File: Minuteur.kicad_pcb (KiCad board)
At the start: 2 copper layers, 149.9 x 49.5 mm, 47 parts, among them J1 ICSP, J2 Screw_Terminal_1x02, J3 Piezo, J4 Inputs, J5 Data, J6 USB_OTG, J7 Screw_Terminal_1x03, J8 Outputs, Q1 BC818-40, SW1 Rotary_Encoder_Switch, SW2 SW_Push_SPDT_2Leds, SW3 SW_Push_SPDT_2Leds, U1 ATMEGA328P-AU, U2 LD1117S50TR, U3 MAX7219, U4 PC817, Y1 16MHz

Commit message: General layout done.
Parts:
- removed AFF1: CC56-12, Displays_7-Segment:Cx56-12
- removed D3: LED, LEDs:LED_0805
- removed D4: D, Diodes_SMD:D_SOD-123
- removed J7: Screw_Terminal_1x03, Connectors:bornier3
- removed J8: Outputs, Pin_Headers:Pin_Header_Straight_1x04_Pitch2.54mm
- removed R11, R12: 470, Resistors_SMD:R_0805
- removed REF** (x4): MountingHole_3.2mm_M3_Pad, Mounting_Holes:MountingHole_3.2mm_M3_Pad
- removed REF** (x2): Fiducial_1mm_Dia_2.54mm_Outer_CopperTop, Fiducials:Fiducial_1mm_Dia_2.54mm_Outer_CopperTop
- removed REF**: Logo_labo_20mm, Logos:Logo_labo_20mm
- removed SW3: SW_Push_SPDT_2Leds, Switches_perso:SP86-THT-PushButton
- added C6: 100n, Capacitor_SMD:C_0805_2012Metric, F.Cu at (189.5, 93.5)
- added FID1: Fiducial, Fiducial:Fiducial_0.75mm_Mask1.5mm, F.Cu at (187.9, 147.0)
- added FID2: Fiducial, Fiducial:Fiducial_0.75mm_Mask1.5mm, F.Cu at (191.0, 147.0)
- added FID3: Fiducial, Fiducial:Fiducial_0.75mm_Mask1.5mm, F.Cu at (194.0, 147.0)
- added FID4: Fiducial, Fiducial:Fiducial_0.75mm_Mask1.5mm, F.Cu at (187.9, 150.1)
- added FID5: Fiducial, Fiducial:Fiducial_0.75mm_Mask1.5mm, F.Cu at (191.0, 150.1)
- added FID6: Fiducial, Fiducial:Fiducial_0.75mm_Mask1.5mm, F.Cu at (187.9, 153.1)
- added H1: MountingHole, MountingHole:MountingHole_3.2mm_M3, F.Cu at (93.0, 72.0)
- added H2: MountingHole, MountingHole:MountingHole_3.2mm_M3, F.Cu at (203.0, 72.0)
- added H3: MountingHole, MountingHole:MountingHole_3.2mm_M3, F.Cu at (203.0, 112.0)
- added H4: MountingHole, MountingHole:MountingHole_3.2mm_M3, F.Cu at (93.0, 112.0)
- added U5: CC56-12EWA, Display_7Segment:CA56-12EWA, B.Cu at (180.0, 93.0)
- C1, C5: footprint Capacitors_SMD:C_0805 -> Capacitor_SMD:C_0805_2012Metric
- C2: value 47u -> 100n; footprint Capacitors_SMD:CP_Elec_6.3x5.3 -> Capacitor_SMD:C_0805_2012Metric
- C3: footprint Capacitors_SMD:CP_Elec_6.3x5.3 -> Capacitor_SMD:CP_Elec_6.3x5.3
- C4: value 100n -> 47u; footprint Capacitors_SMD:C_0805 -> Capacitor_SMD:CP_Elec_6.3x5.3
- D1: footprint Diodes_SMD:D_SOD-123 -> Diode_SMD:D_SOD-123
- D2: value LED -> D; footprint LEDs:LED_0805 -> Diode_SMD:D_SOD-123
- J1: value ICSP -> Screw_Terminal_01x02; footprint Connectors:IDC_Header_Straight_6pins -> Connector_Phoenix_MSTB:PhoenixContact_MSTBVA_2,5_2-G-5,08_1x02_P5.08mm_Vertical
- J2: value Screw_Terminal_1x02 -> ICSP; footprint Connectors:bornier2 -> Connector_PinHeader_2.54mm:PinHeader_2x03_P2.54mm_Vertical
- J3: value Piezo -> piezo; footprint Pin_Headers:Pin_Header_Straight_1x02_Pitch2.54mm -> Connector_PinHeader_2.54mm:PinHeader_1x02_P2.54mm_Vertical
- J4: value Inputs -> Conn_01x10; footprint Pin_Headers:Pin_Header_Straight_1x07_Pitch2.54mm -> Connector_PinHeader_2.54mm:PinHeader_1x10_P2.54mm_Vertical
- J5: value Data -> output; footprint Pin_Headers:Pin_Header_Straight_1x06_Pitch2.54mm -> Connector_PinHeader_2.54mm:PinHeader_1x04_P2.54mm_Vertical
- J6: value USB_OTG -> Screw_Terminal_01x03; footprint Connectors:USB_Micro-B -> Connector_Phoenix_MSTB:PhoenixContact_MSTBVA_2,5_3-G-5,08_1x03_P5.08mm_Vertical
- Q1: value BC818-40 -> BC818; footprint TO_SOT_Packages_SMD:SOT-23 -> Package_TO_SOT_SMD:SOT-23
- R1, R4: footprint Resistors_SMD:R_0805 -> Resistor_SMD:R_0805_2012Metric
- R10: value 510 -> 470; footprint Resistors_SMD:R_0805 -> Resistor_SMD:R_0805_2012Metric
- R2: value 10K -> 10k; footprint Resistors_SMD:R_0805 -> Resistor_SMD:R_0805_2012Metric
- R3: value 1K -> 470; footprint Resistors_SMD:R_0805 -> Resistor_SMD:R_0805_2012Metric
- R5: value 470 -> 30k; footprint Resistors_SMD:R_0805 -> Resistor_SMD:R_0805_2012Metric
- R6: value 30K -> 470; footprint Resistors_SMD:R_0805 -> Resistor_SMD:R_0805_2012Metric
- R7: value 470 -> 1k; footprint Resistors_SMD:R_0805 -> Resistor_SMD:R_0805_2012Metric
- R8: value 1K -> 1k; footprint Resistors_SMD:R_0805 -> Resistor_SMD:R_0805_2012Metric
- R9: value 1K -> 510; footprint Resistors_SMD:R_0805 -> Resistor_SMD:R_0805_2012Metric
- RL1: footprint Relays_THT:Relay_SPDT_SANYOU_SRD_Series_Form_C -> Relay_THT:Relay_SPDT_SANYOU_SRD_Series_Form_C; moved to F.Cu
- SW1: footprint Switches_perso:EC12_switch-RotaryEncoder -> Rotary_Encoder:RotaryEncoder_Alps_EC12E-Switch_Vertical_H20mm_CircularMountingHoles; moved to B.Cu
- SW2: footprint Switches_perso:SP86-THT-PushButton -> Switch_Perso:SP86-THT-PushButton; moved to B.Cu
- U1: value ATMEGA328P-AU -> ATmega328P-AU; footprint Housings_QFP:TQFP-32_7x7mm_Pitch0.8mm -> Package_QFP:TQFP-32_7x7mm_P0.8mm
- U2: value LD1117S50TR -> LD1117S50TR_SOT223; footprint TO_SOT_Packages_SMD:SOT-223-3Lead_TabPin2 -> Package_TO_SOT_SMD:SOT-223-3_TabPin2
- U3: footprint Housings_SOIC:SOIC-24W_7.5x15.4mm_Pitch1.27mm -> Package_SO:SOIC-24W_7.5x15.4mm_P1.27mm
- U4: footprint Housings_DIP:DIP-4_W7.62mm_SMD -> Package_DIP:DIP-4_W7.62mm
- Y1: footprint SMD_perso:Resonator_SMD-3pin_3213 -> Crystal:Resonator_SMD_muRata_CSTxExxV-3Pin_3.0x1.1mm
- moved J6 120.6 mm to (193.0, 110.0), turned to 180 degrees
- moved R10 81.5 mm to (104.8, 88.5), turned to 270 degrees
- moved C2 76.4 mm to (157.5, 85.0), turned to 0 degrees
- moved J2 72.3 mm to (139.0, 73.2), turned to 90 degrees
- moved U3 54.1 mm to (195.0, 85.5), turned to 270 degrees
- moved J3 52.1 mm to (116.0, 79.0), turned to 0 degrees
- moved R5 51.4 mm to (205.6, 82.5), turned to 0 degrees
- moved J5 49.9 mm to (112.9, 70.8), turned to 90 degrees
- moved J4 46.7 mm to (162.2, 70.8), turned to 90 degrees
- moved R2 41.9 mm to (149.5, 72.1), turned to 270 degrees
- moved R1 41.2 mm to (116.0, 89.0), turned to 0 degrees
- moved SW1 40.5 mm to (127.2, 78.2), turned to 270 degrees
- moved D1 39.7 mm to (147.0, 72.0)
- moved U4 38.5 mm to (139.2, 99.8), turned to 0 degrees
- moved D2 37.7 mm to (153.0, 107.0), turned to 90 degrees
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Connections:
- C1 pad 1: GND -> +5V
- C1 pad 2: +5V -> GND
- C2 pad 1: VCC -> +5V
- C3 pad 1: +5V -> +12V
- C5 pad 1: GND -> +5V
- C5 pad 2: +5V -> GND
- D2 pad 1: Net-(D2-Pad1) -> +5V
- D2 pad 2: +5V -> Net-(D2-Pad2)
- J1 pad 1: MISO -> +12V
- J1 pad 2: +5V -> GND
- J2 pad 1: GND -> MISO
- J2 pad 2: VCC -> +5V
- J4 pad 1: BTN_3 -> D0
- J4 pad 2: ENC_B -> D1
- J4 pad 3: ENC_A -> D6
- J4 pad 4: BTN_2 -> A3
- J4 pad 5: BTN_1 -> A4
- J4 pad 6: +5V -> A5
- J4 pad 7: GND -> A6
- J5 pad 1: TXD -> OUT_2
- J5 pad 2: RXD -> OUT_1
- J5 pad 3: SDA -> +5V
- J5 pad 4: SCL -> GND
- J6 pad 1: +5V -> Net-(J6-Pad1)
- J6 pad 2: (no net) -> Net-(J6-Pad2)
- J6 pad 3: (no net) -> GND
- Q1 pad 3: Net-(D4-Pad2) -> Net-(D2-Pad2)
- R10 pad 1: Net-(R10-Pad1) -> BTN_1
- R10 pad 2: Net-(Q1-Pad1) -> Net-(R10-Pad2)
- R3 pad 1: Net-(D2-Pad1) -> Net-(R3-Pad1)
- R3 pad 2: GND -> ENC_A
- R4 pad 2: ENC_A -> ENC_B
- R5 pad 1: Net-(R5-Pad1) -> +5V
- R5 pad 2: ENC_B -> Net-(R5-Pad2)
- R6 pad 1: +5V -> BTN_2
- R7 pad 1: BTN_3 -> OUT_1
- R7 pad 2: Net-(R7-Pad2) -> +5V
- R8 pad 1: +5V -> Net-(R8-Pad1)
- R8 pad 2: OUT_1 -> +5V
- R9 pad 1: +5V -> Net-(Q1-Pad1)
- RL1 pad 1: Net-(J7-Pad2) -> +12V
- RL1 pad 3: Net-(J7-Pad3) -> Net-(J6-Pad2)
- RL1 pad 4: Net-(J7-Pad1) -> Net-(J6-Pad1)
- RL1 pad 5: Net-(D4-Pad2) -> Net-(D2-Pad2)
- SW2 pad 3: Net-(R11-Pad2) -> Net-(R10-Pad2)
- U1 pad 10: BTN_3 -> D6
- U1 pad 19: (no net) -> A6
- U1 pad 22: (no net) -> A7
- U1 pad 26: (no net) -> A3
- U1 pad 27: SDA -> A4
- U1 pad 28: SCL -> A5
- U1 pad 30: RXD -> D0
- U1 pad 31: TXD -> D1
- U2 pad 3: VCC -> +12V
- U3 pad 18: Net-(R6-Pad2) -> Net-(R5-Pad2)
- U4 pad 1: Net-(R9-Pad2) -> Net-(R8-Pad1)
- U4 pad 2: Net-(D3-Pad2) -> OUT_1
- U4 pad 3: Net-(R10-Pad1) -> Net-(R9-Pad2)
- Y1 pad 1: Net-(U1-Pad7) -> Net-(U1-Pad8)
- Y1 pad 3: Net-(U1-Pad8) -> Net-(U1-Pad7)
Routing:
- net +5V: track 292.7 -> 20.5 mm, vias 12 -> 0
- net GND: track 192.6 -> 29.1 mm, vias 24 -> 0
- net BTN_1: track 142.0 -> 0.00 mm, vias 1 -> 0
- net ENC_A: track 104.0 -> 0.00 mm, vias 2 -> 0
- net BTN_3: track 96.6 -> 0.00 mm, vias 2 -> 0
- net ENC_B: track 94.9 -> 0.00 mm, vias 4 -> 0
- net BTN_2: track 89.5 -> 0.00 mm, vias 3 -> 0
- net OUT_1: track 54.6 -> 0.00 mm, vias 1 -> 0
- net +12V: track 0.00 -> 49.1 mm
- net SCL: track 45.1 -> 0.00 mm, vias 2 -> 0
- net Net-(J7-Pad2): track 45.1 -> 0.00 mm
- net OUT_2: track 44.6 -> 0.00 mm
- net SDA: track 42.1 -> 0.00 mm, vias 2 -> 0
- net dig_0: track 38.2 -> 0.00 mm, vias 1 -> 0
- net RXD: track 34.2 -> 0.00 mm, vias 1 -> 0
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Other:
- board size 149.9 x 49.5 mm -> 120 x 50 mm
- net class 12VCC added: clearance 1, trace_width 3, via_dia 0.6, via_drill 0.4
- net class AC240 removed
- net class Default: clearance 0.25 -> 0.2; trace_width 0.5 -> 0.25
- net class VCC removed
- rule trace_clearance: 0.25 -> 0.2
- rule trace_min: 0.25 -> 0.2
- board text removed: "5V"
- board text removed: "BTN 1"
- board text removed: "BTN 2"
- board text removed: "BTN 3"
- board text removed: "COM"
- board text removed: "ENC A"
- board text removed: "ENC B"
- board text removed: "GND"
- board text removed: "MISO"
- board text removed: "MOSI"
- board text removed: "Minuteur v1"
- board text removed: "NC"
- board text removed: "NO"
- board text removed: "O1"
- board text removed: "O2"
- board text removed: "ON"
- board text removed: "RST"
- board text removed: "RX"
- board text removed: "SCK"
- board text removed: "SCL"
- board text removed: "SDA"
- board text removed: "TX"
- board text removed: "VCC"
- board text removed: "https://www.lelabodutroisieme.fr 09/2017"

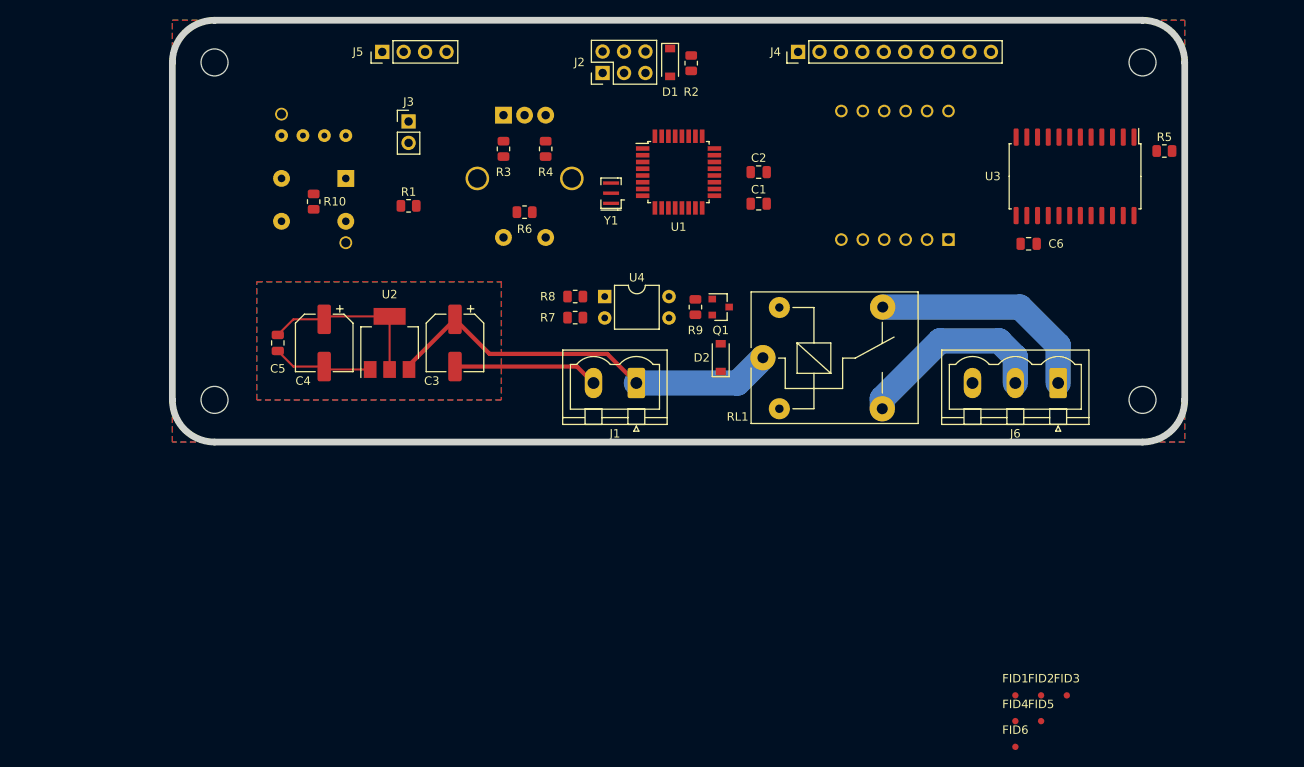
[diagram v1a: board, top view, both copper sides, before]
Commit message: Routing done. Maybe need to move down extension connectors a little. Also need to replace the piezo connector by a SMD one.
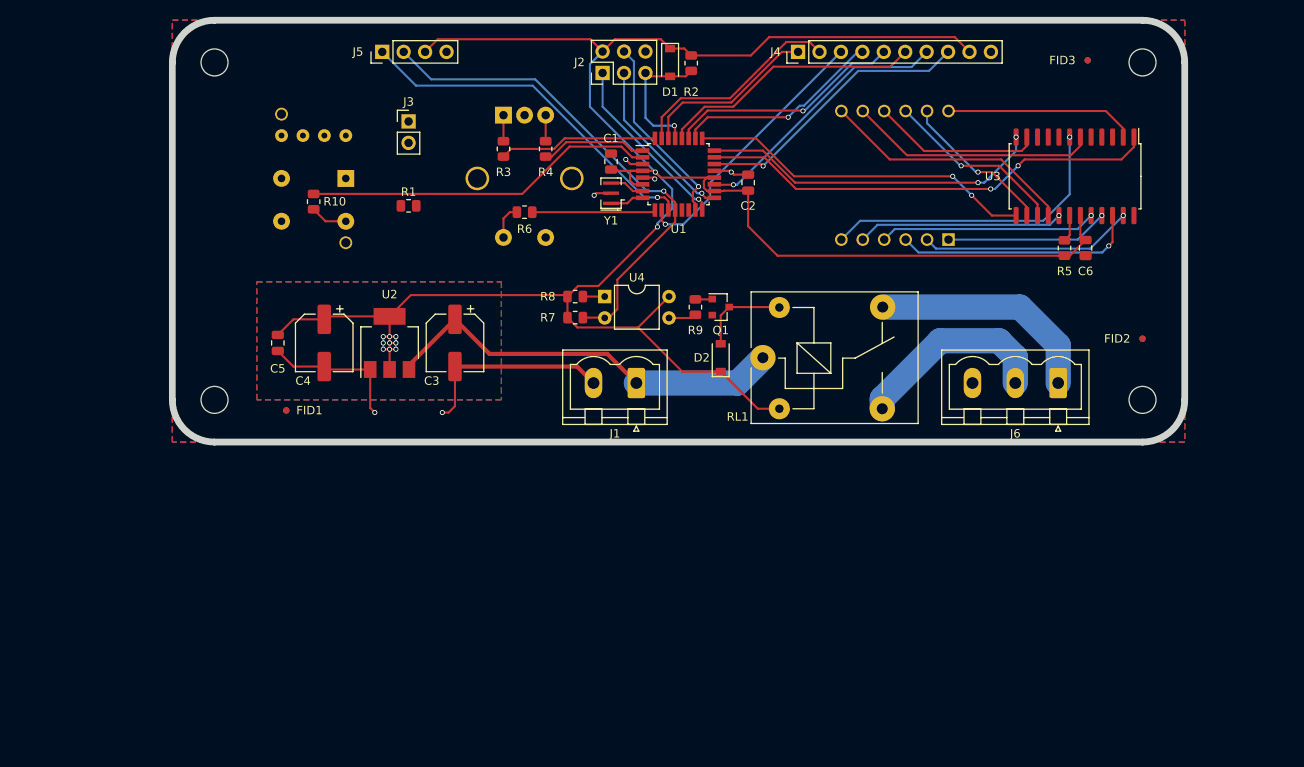
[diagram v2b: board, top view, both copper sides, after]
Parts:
- FID4, FID5, FID6: moved to B.Cu
- moved FID4 93.9 mm to (101.5, 113.2)
- moved FID1 92.8 mm to (101.5, 113.2)
- moved FID6 81.8 mm to (196.5, 71.8)
- moved FID3 75.3 mm to (196.5, 71.8)
- moved FID5 46.9 mm to (203.0, 104.8)
- moved FID2 44.0 mm to (203.0, 104.8)
- moved C1 18.2 mm to (140.0, 83.8), turned to 90 degrees
- moved R5 16.5 mm to (193.8, 94.0), turned to 90 degrees
- moved C6 6.77 mm to (196.2, 94.0), turned to 270 degrees
- moved C2 1.77 mm to (156.2, 86.2), turned to 90 degrees
- moved U1 0.25 mm to (148.0, 85.2)
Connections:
- R10 pad 1: BTN_1 -> BTN_2
- R6 pad 1: BTN_2 -> BTN_1
- U1 pad 2: BTN_1 -> BTN_2
- U1 pad 9: BTN_2 -> BTN_1
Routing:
- net +5V: track 20.5 -> 270.0 mm, vias 0 -> 11
- net OUT_1: track 0.00 -> 59.6 mm, vias 0 -> 1
- net MAX_DATA: track 0.00 -> 54.5 mm, vias 0 -> 2
- net OUT_2: track 0.00 -> 42.3 mm, vias 0 -> 1
- net BTN_2: track 0.00 -> 41.9 mm
- net MAX_CLK: track 0.00 -> 41.0 mm, vias 0 -> 2
- net MAX_LOAD: track 0.00 -> 40.5 mm, vias 0 -> 2
- net dig_3: track 0.00 -> 36.1 mm, vias 0 -> 1
- net A7: track 0.00 -> 33.4 mm, vias 0 -> 1
- net D6: track 0.00 -> 32.2 mm, vias 0 -> 1
- net A6: track 0.00 -> 31.7 mm, vias 0 -> 1
- net A5: track 0.00 -> 31.3 mm
- net seg_B: track 0.00 -> 30.3 mm
- net dig_2: track 0.00 -> 29.5 mm
- net seg_DP: track 0.00 -> 28.8 mm, vias 0 -> 1
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
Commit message: All routing done, DRC ok.
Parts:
- removed J3: piezo, Connector_PinHeader_2.54mm:PinHeader_1x02_P2.54mm_Vertical
- added U6: Piezo_sounder, IC_Perso:Murata_PKMCS0909_xxxxx, F.Cu at (116.6, 90.5)
- R1: value 470 -> 1k
- R8: value 1k -> 470
- moved R1 7.52 mm to (116.5, 96.5)
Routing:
- net PIEZO_1: track 0.00 -> 35.7 mm, vias 0 -> 2
- net PIEZO_2: track 0.00 -> 33.2 mm, vias 0 -> 2
- net Net-(R1-Pad1): track 0.00 -> 7.38 mm
- net GND: track 50.9 -> 44.4 mm, vias 6 -> 5
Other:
- board text added: "12V"
- board text added: "GND"
- board text added: "NC"
- board text added: "NO"

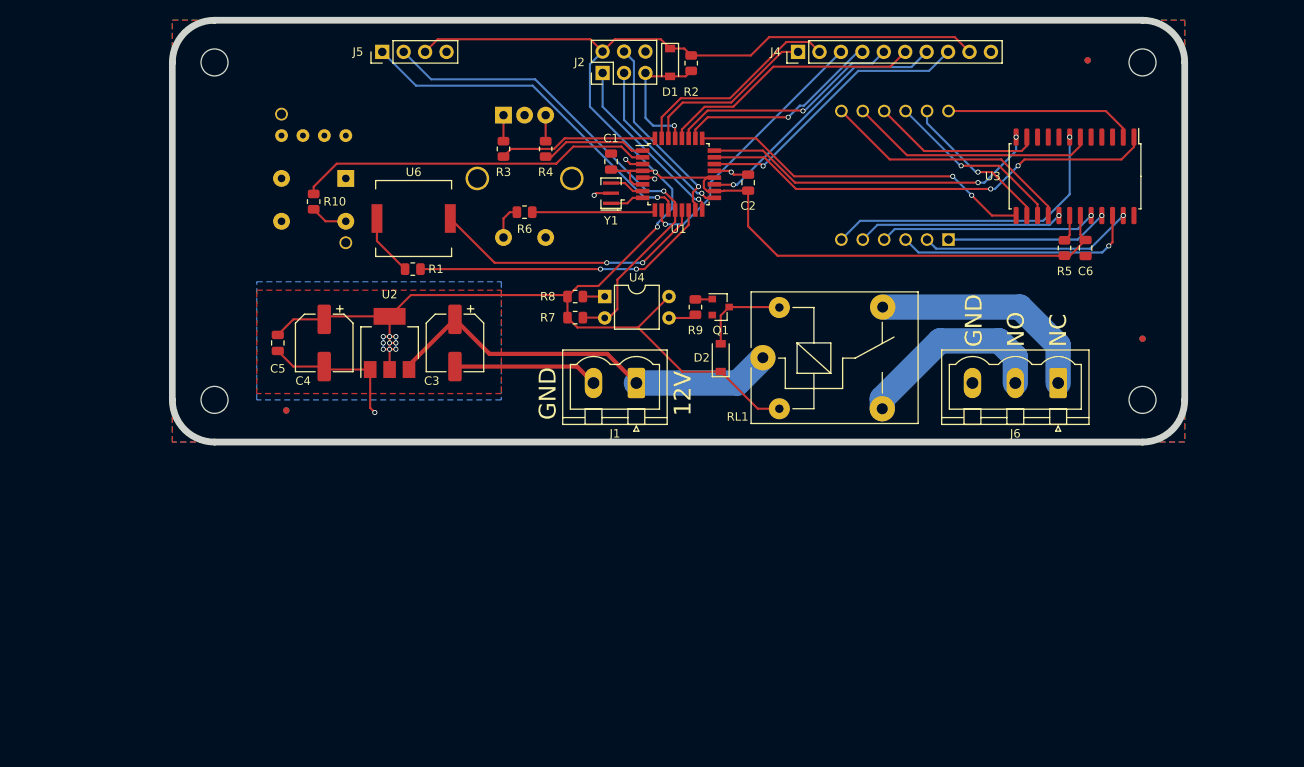
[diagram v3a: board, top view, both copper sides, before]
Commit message: Smaller version (100x50mm) routed. optocoupler changed. R-serie resistance for optocoupler changed to 200Ohm, so the optocoupler is in saturated region. Power lines have been changed from 0.25 to 0.5 width?
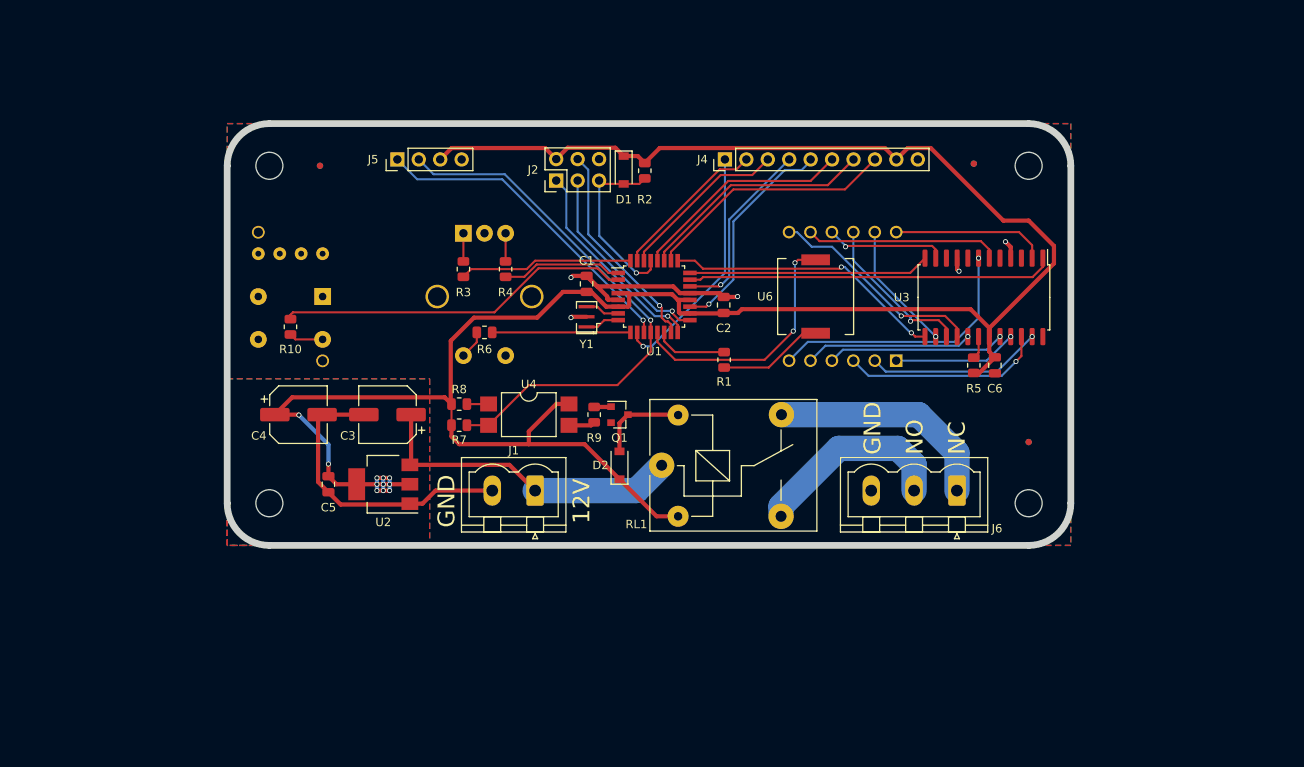
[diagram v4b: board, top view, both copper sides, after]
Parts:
- R8: value 470 -> 200
- U4: value PC817 -> LTV-817S; footprint Package_DIP:DIP-4_W7.62mm -> Package_DIP:SMDIP-4_W9.53mm
- moved U6 48.5 mm to (164.2, 99.8), turned to 90 degrees
- moved R1 38.4 mm to (153.4, 107.2), turned to 90 degrees
- moved FID1 29.3 mm to (105.5, 84.2)
- moved FID4 29.3 mm to (105.5, 84.2)
- moved R7 18.8 mm to (122.0, 115.0)
- moved R8 18.8 mm to (122.0, 112.5)
- moved FID2 18.2 mm to (189.5, 117.0)
- moved FID3 18.2 mm to (183.0, 84.0)
- moved FID5 18.2 mm to (189.5, 117.0)
- moved FID6 18.2 mm to (183.0, 84.0)
- moved H2 18.2 mm to (189.5, 84.2)
- moved H3 18.2 mm to (189.5, 124.2)
- moved U3 18.0 mm to (184.2, 99.8)
- moved C5 17.8 mm to (106.5, 122.0)
- moved C6 17.6 mm to (185.5, 107.9)
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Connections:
- J4 pad 1: D0 -> D6
- J4 pad 3: D6 -> D0
- J4 pad 4: A3 -> A7
- J4 pad 5: A4 -> A6
- J4 pad 7: A6 -> A4
- J4 pad 8: A7 -> A3
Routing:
- net PIEZO_1: track 35.7 -> 8.68 mm, vias 2 -> 0
- net GND: track 44.4 -> 67.3 mm
- net MAX_LOAD: track 40.5 -> 28.6 mm, vias 2 -> 0
- net A7: track 33.4 -> 22.0 mm
- net MAX_DATA: track 54.5 -> 43.5 mm, vias 2 -> 0
- net +12V: track 49.1 -> 38.4 mm
- net +5V: track 270.0 -> 277.8 mm
- net MAX_CLK: track 41.0 -> 33.2 mm
- net D1: track 25.4 -> 18.5 mm
- net dig_2: track 29.5 -> 23.1 mm
- net A6: track 31.7 -> 25.7 mm
- net dig_1: track 20.2 -> 14.3 mm, vias 0 -> 1
- net Net-(R1-Pad1): track 7.38 -> 12.5 mm
- net A3: track 24.7 -> 29.8 mm, vias 1 -> 0
- net A5: track 31.3 -> 26.3 mm
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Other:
- board size 120 x 50 mm -> 100 x 50 mm
- net class PWR added: clearance 0.25, trace_width 0.5, via_dia 0.6, via_drill 0.4

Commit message: AC version ready for fab.
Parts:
- removed the C3 at (113.5, 113.8)
- removed C4: 47u, Capacitor_SMD:CP_Elec_6.3x5.3
- removed C5: 100n, Capacitor_SMD:C_0805_2012Metric
- removed J1: Screw_Terminal_01x02, Connector_Phoenix_MSTB:PhoenixContact_MSTBVA_2,5_2-G-5,08_1x02_P5.08mm_Vertical
- removed the U2 at (113.0, 122.0)
- added ICSP: ICSP, Connector_PinHeader_2.54mm:PinHeader_2x03_P2.54mm_Vertical, F.Cu at (133.5, 86.0)
- added REF**: Logo_labo_5mm, Logo:Logo_labo_5mm, F.Cu at (117.2, 101.2)
- J2: value ICSP -> USB_B_Micro; footprint Connector_PinHeader_2.54mm:PinHeader_2x03_P2.54mm_Vertical -> Connector_USB:USB_Micro-B_Amphenol_10118194_Horizontal
- moved J2 45.5 mm to (97.7, 114.1), turned to 270 degrees
- renumbered C6 to C3, J4 to I/O, J6 to J5, U6 to U2, J5 to output
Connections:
- J2 pad 1: MISO -> +5V
- J2 pad 2: +5V -> (no net)
- J2 pad 3: SCK -> (no net)
- J2 pad 4: MOSI -> (no net)
- J2 pad 5: RESET -> GND
- J5 pad 2: Net-(J6-Pad2) -> Net-(J5-Pad2)
- J5 pad 3: GND -> Net-(J5-Pad3)
- RL1 pad 1: +12V -> Net-(J5-Pad2)
- RL1 pad 3: Net-(J6-Pad2) -> Net-(J5-Pad3)
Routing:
- net Net-(J5-Pad2): track 0.00 -> 65.5 mm
- net +5V: track 277.8 -> 228.0 mm, vias 11 -> 2
- net +12V: track 38.4 -> 0.00 mm
- net GND: track 67.3 -> 43.1 mm, vias 5 -> 7
- net Net-(J5-Pad1): track 27.1 -> 51.1 mm
- net Net-(J5-Pad3): track 0.00 -> 23.9 mm
- net Net-(J6-Pad2): track 23.7 -> 0.00 mm
- removed copper zone on B.Cu, net +5V
- removed copper zone on F.Cu, net +5V
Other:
- outline, holes or cut-outs redrawn
- net class 12VCC removed
- net class VAC added: clearance 1, trace_width 3, via_dia 0.6, via_drill 0.4
- rule pad_to_mask_clearance: 0.2 -> 0
- board text added: "12/2020"
- board text added: "5V"
- board text added: "A3"
- board text added: "A4"
- board text added: "A5"
- board text added: "A6"
- board text added: "A7"
- board text added: "COM"
- board text added: "D0"
- board text added: "D1"
- board text added: "D6"
- board text added: "JLCJLCJLCJLC"
- board text added: "Minuteur V2.0"
- board text added: "out 1"
- board text added: "out 2"
- board text added: "www.lelabodutroisieme.fr"
- board text removed: "12V"
